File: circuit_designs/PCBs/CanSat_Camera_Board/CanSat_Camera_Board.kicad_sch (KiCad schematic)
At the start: 3 parts

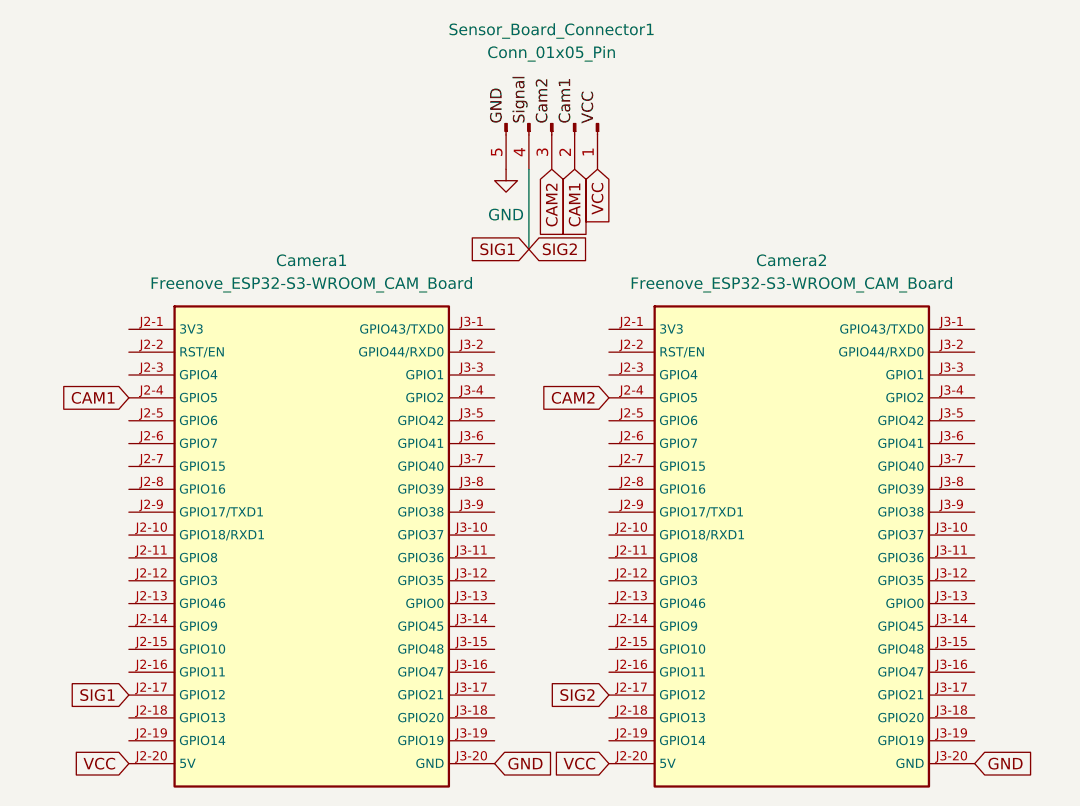
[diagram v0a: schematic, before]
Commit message: Updating camera and sensor PCBs
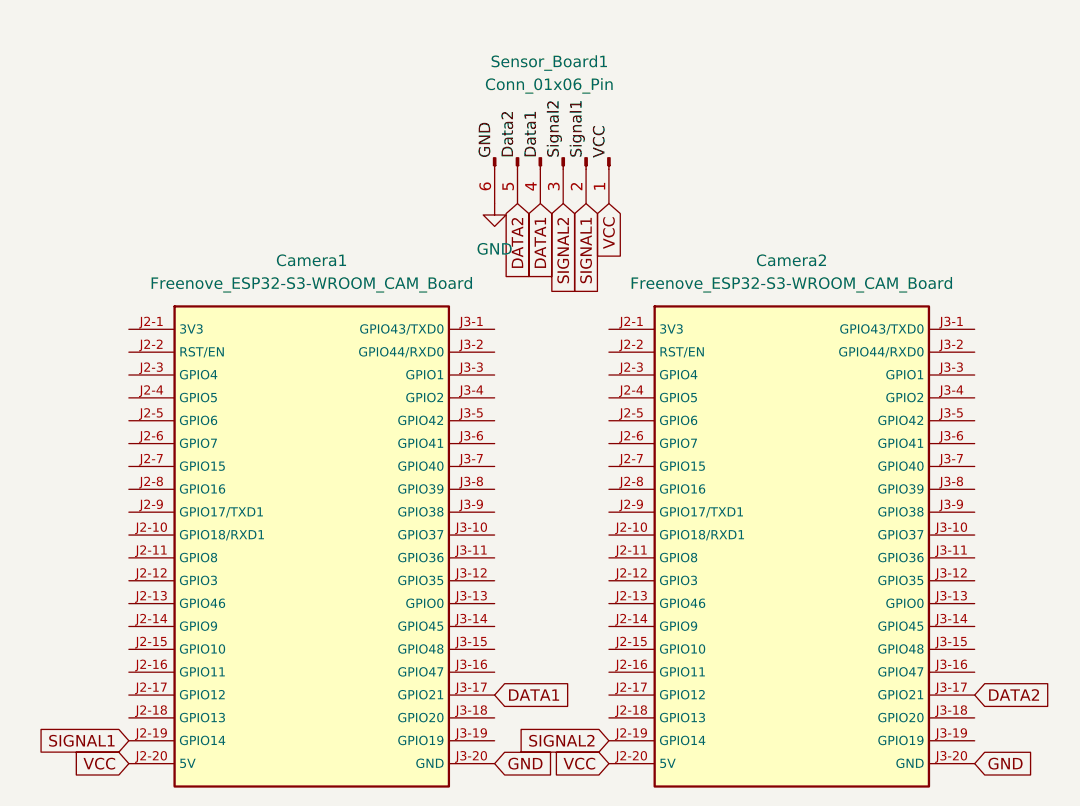
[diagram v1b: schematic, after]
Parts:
- removed Sensor_Board_Connector1: Conn_01x05_Pin, Connector_JST:JST_PH_B5B-PH-K_1x05_P2.00mm_Vertical, symbol Connector:Conn_01x05_Pin
- added Sensor_Board1: Conn_01x06_Pin, Connector_JST:JST_PH_B6B-PH-K_1x06_P2.00mm_Vertical, symbol Connector:Conn_01x06_Pin
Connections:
- net GND: now also Sensor_Board1.6 (Pin_6)
- net VCC: now also Sensor_Board1.1 (Pin_1)
- net SIGNAL2: now reaches Camera2.J2-19 (GPIO14)
- net SIGNAL2: now also Sensor_Board1.3 (Pin_3)
- net DATA2: now reaches Camera2.J3-17 (GPIO21)
- net DATA2: now also Sensor_Board1.5 (Pin_5)
- net SIGNAL1: now reaches Camera1.J2-19 (GPIO14)
- net SIGNAL1: now also Sensor_Board1.2 (Pin_2)
- net DATA1: now reaches Camera1.J3-17 (GPIO21)
- net DATA1: now also Sensor_Board1.4 (Pin_4)
- net CAM1: no longer names the net of Camera1.J2-4 (GPIO5)
- net CAM2: no longer names the net of Camera2.J2-4 (GPIO5)
- net SIG1: no longer names the net of Camera2.J2-17 (GPIO12)
- net SIG1: no longer Camera1.J2-17 (GPIO12)

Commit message: Final review submission of all CanSat PCB boards and corresponding custom KiCad 3D models, footprints, and symbols
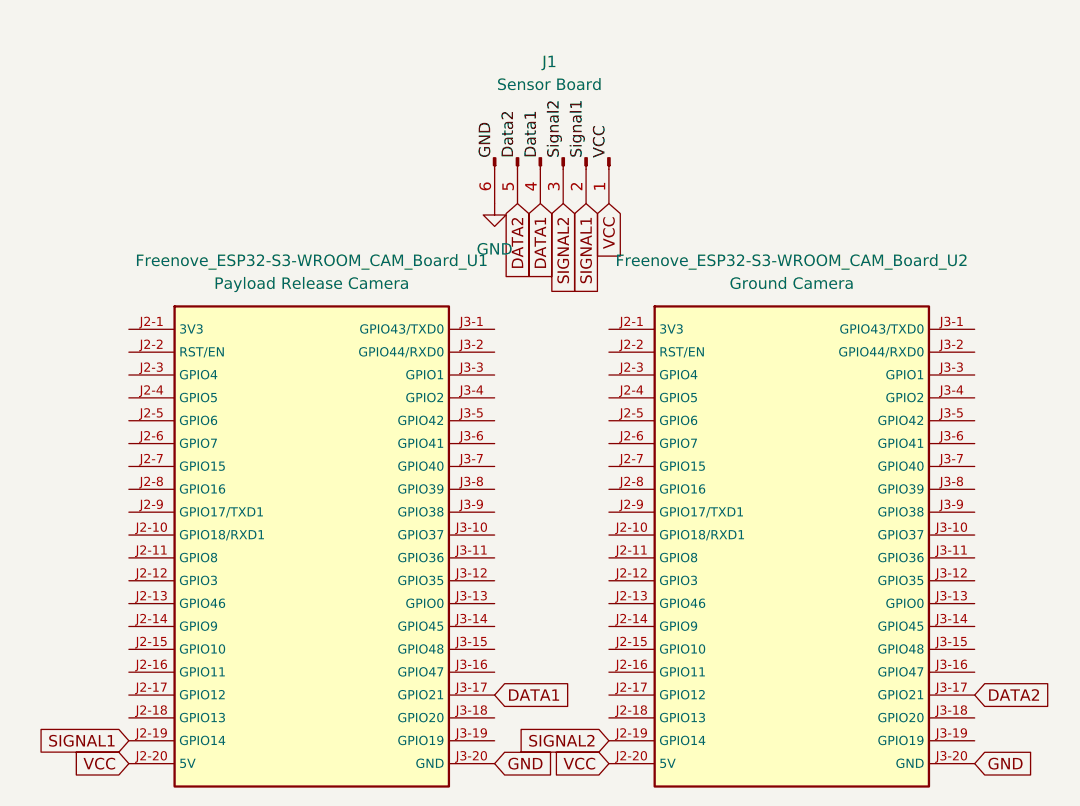
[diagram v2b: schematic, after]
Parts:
- Freenove_ESP32-S3-WROOM_CAM_Board_U1: renamed from Camera1; value Freenove_ESP32-S3-WROOM_CAM_Board -> Payload Release Camera
- Freenove_ESP32-S3-WROOM_CAM_Board_U2: renamed from Camera2; value Freenove_ESP32-S3-WROOM_CAM_Board -> Ground Camera
- J1: renamed from Sensor_Board1; value Conn_01x06_Pin -> Sensor Board
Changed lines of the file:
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@@
 		(dnp no)
 		(fields_autoplaced yes)
-		(property "Reference" "Camera2"
+		(property "Reference" "Freenove_ESP32-S3-WROOM_CAM_Board_U2"
 			(at 176.53 81.28 0)
 			(effects
@@
 			)
 		)
-		(property "Value" "Freenove_ESP32-S3-WROOM_CAM_Board"
+		(property "Value" "Ground Camera"
 			(at 176.53 83.82 0)
 			(effects
@@
 			(project ""
 				(path "/2029a1a1-e60a-46bb-ada1-4fb8088dfb98"
-					(reference "Camera2")
+					(reference "Freenove_ESP32-S3-WROOM_CAM_Board_U2")
 					(unit 1)
 				)
@@
 		(on_board yes)
 		(dnp no)
-		(property "Reference" "Sensor_Board1"
+		(property "Reference" "J1"
 			(at 149.606 59.182 90)
 			(effects
@@
 			)
 		)
-		(property "Value" "Conn_01x06_Pin"
+		(property "Value" "Sensor Board"
 			(at 149.606 61.722 90)
 			(effects
@@
 			(project ""
 				(path "/2029a1a1-e60a-46bb-ada1-4fb8088dfb98"
-					(reference "Sensor_Board1")
+					(reference "J1")
 					(unit 1)
 				)
@@
 		(dnp no)
 		(fields_autoplaced yes)
-		(property "Reference" "Camera1"
+		(property "Reference" "Freenove_ESP32-S3-WROOM_CAM_Board_U1"
 			(at 123.19 81.28 0)
 			(effects
@@
 			)
 		)
-		(property "Value" "Freenove_ESP32-S3-WROOM_CAM_Board"
+		(property "Value" "Payload Release Camera"
 			(at 123.19 83.82 0)
 			(effects
@@
 			(project ""
 				(path "/2029a1a1-e60a-46bb-ada1-4fb8088dfb98"
-					(reference "Camera1")
+					(reference "Freenove_ESP32-S3-WROOM_CAM_Board_U1")
 					(unit 1)
 				)
